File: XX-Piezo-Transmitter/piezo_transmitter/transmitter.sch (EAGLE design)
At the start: 5 parts, among them U1 BD6221FSOP, U2 ATTINY24A-SSUR

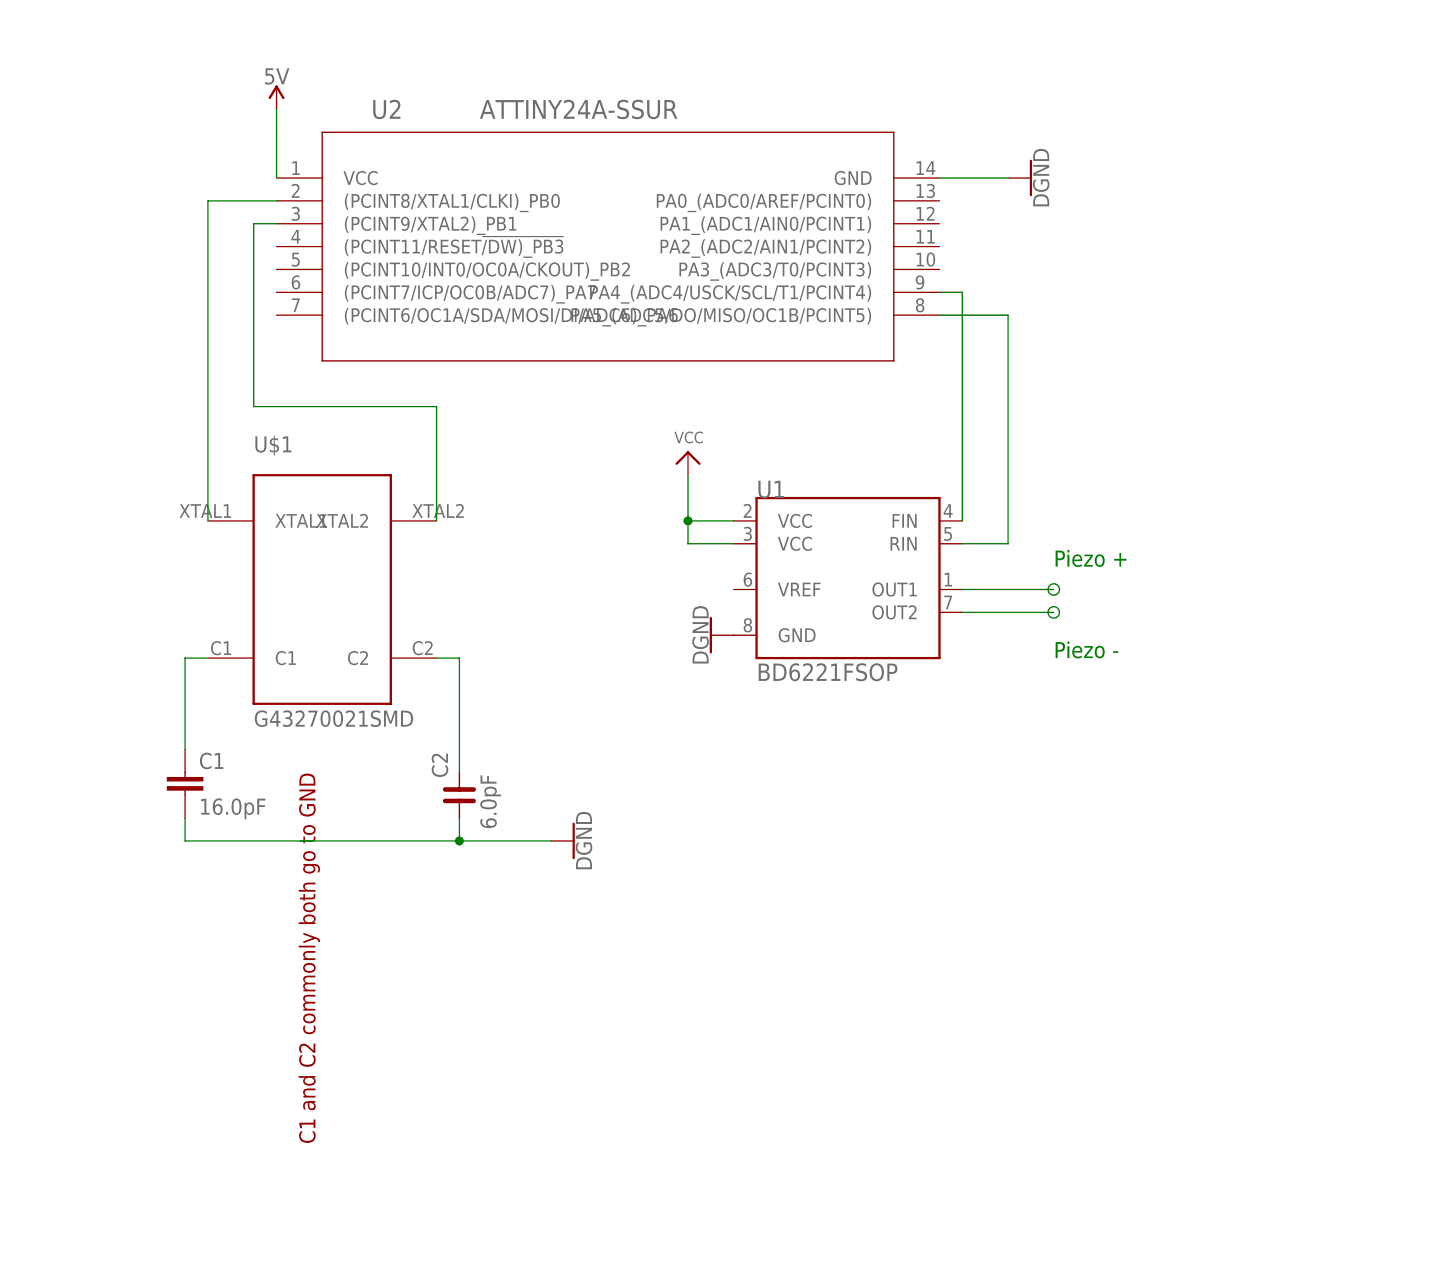
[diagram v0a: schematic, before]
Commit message: Added pin headers & pwm line, crystal and caps change.
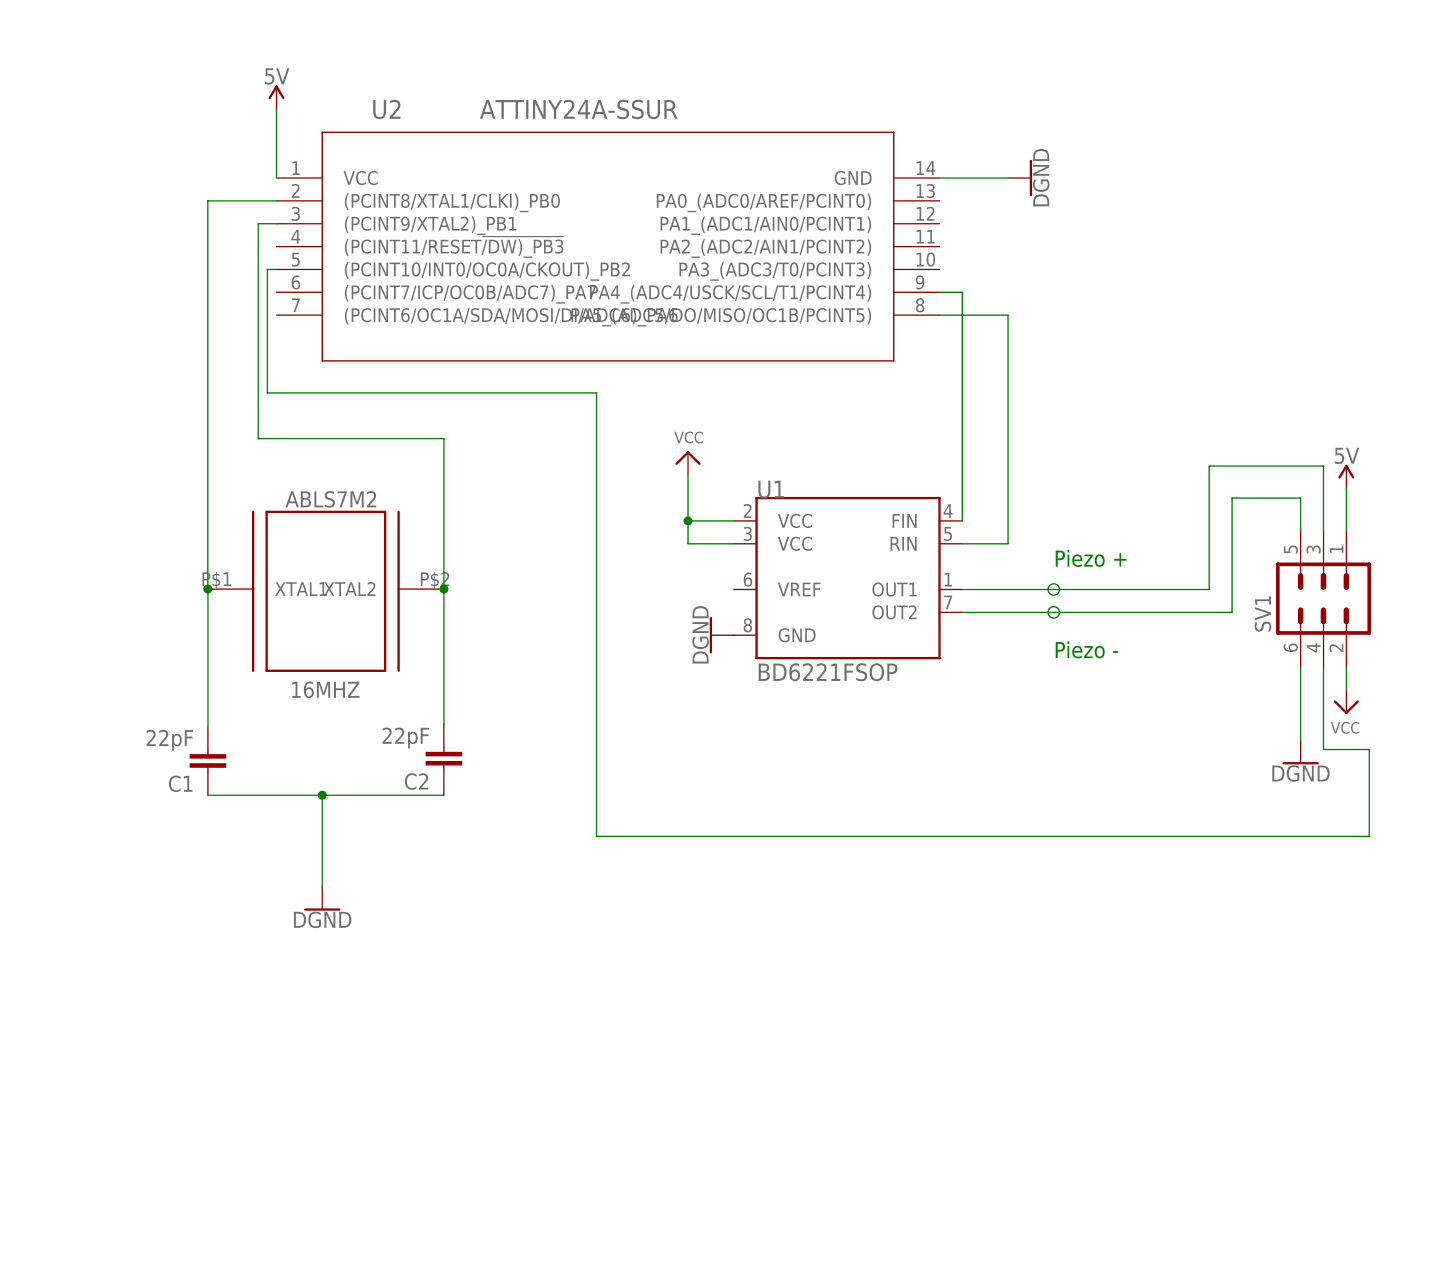
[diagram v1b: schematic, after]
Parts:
- added SV1: (no value), con-lstb:MA03-2
- C1: value 16.0pF -> 22pF; device SparkFun-Capacitors:9.0PF-0603-50V-10% -> SparkFun-Capacitors:22UF-0805-6.3V-20%
- C2: value 6.0pF -> 22pF; device rc-master-smd:C_0201 -> SparkFun-Capacitors:22UF-0805-6.3V-20%
- U$1: value G43270021SMD -> ABLS7M2-16; device G43270021 Oscillator:G43270021SMD -> ABLS7M2-16:ABLS7M2-16
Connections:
- net N$6 renamed FIN
- net N$7 renamed RIN
- removed net C1: C1.1, U$1.C1
- removed net C2: C2.2, U$1.C2
- removed net N$1: U$1.XTAL1, U2.(PCINT8/XTAL1/CLKI)_PB0
- removed net N$2: U$1.XTAL2, U2.(PCINT9/XTAL2)_PB1
- removed net N$5: U2.VCC
- removed net N$8: U1.OUT1
- removed net N$9: U1.OUT2
- new net PIEZO+: SV1.3, U1.OUT1
- new net PIEZO-: SV1.5, U1.OUT2
- new net PWM: SV1.4, U2.(PCINT10/INT0/OC0A/CKOUT)_PB2
- new net VCC_2: SV1.1, U2.VCC
- new net XTAL1: C1.2, U$1.XTAL1, U2.(PCINT8/XTAL1/CLKI)_PB0
- new net XTAL2: C2.2, U$1.XTAL2, U2.(PCINT9/XTAL2)_PB1
- net GND: now also C1.1, SV1.6; no longer C1.2
- net VCC: now also SV1.2
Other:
- moved on the sheet: C1, C2

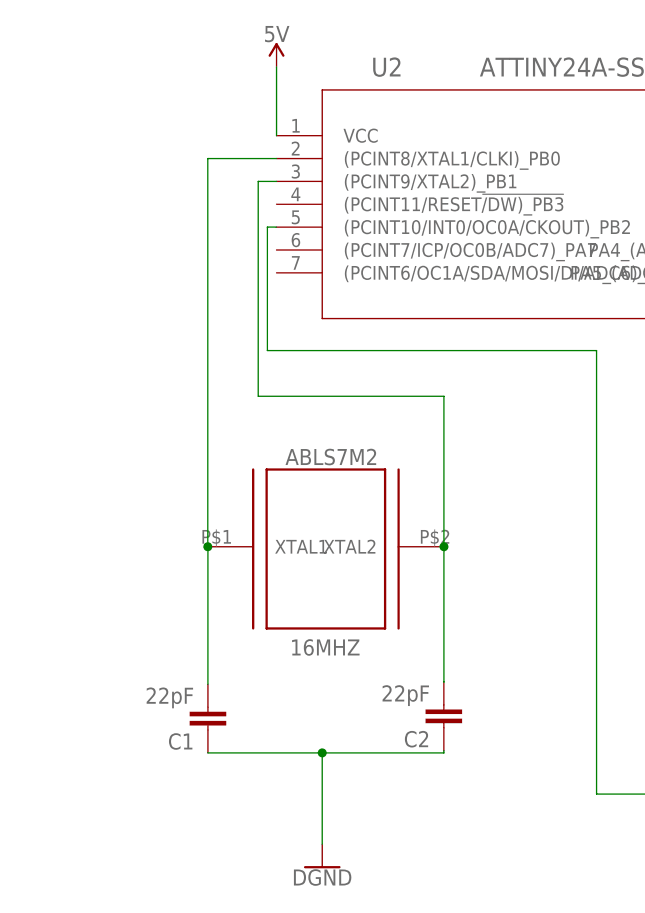
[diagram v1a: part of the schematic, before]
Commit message: Change to through hole crystal. Change to LV 22pf cap.
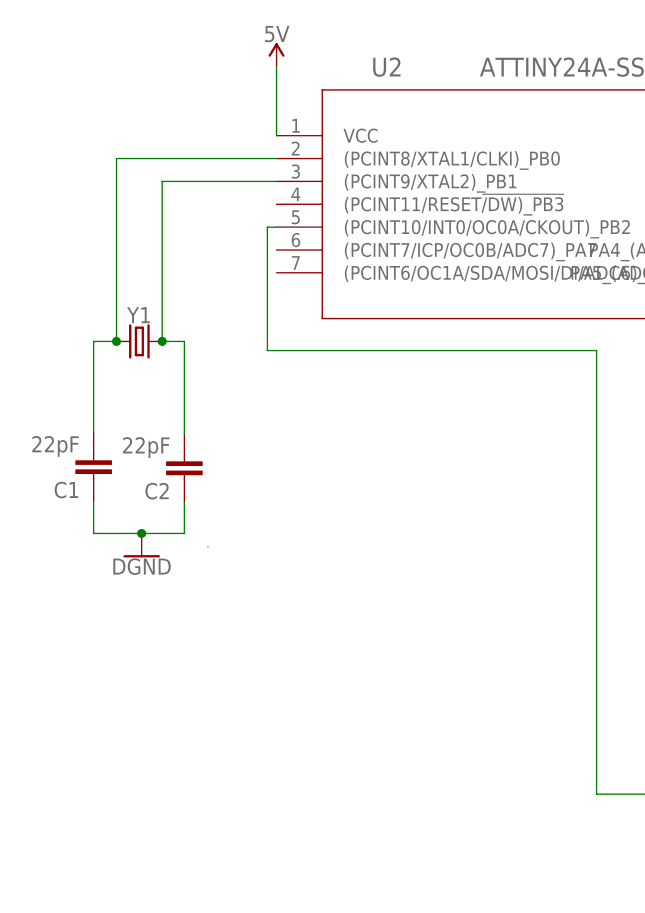
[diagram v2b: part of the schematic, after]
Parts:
- removed U$1: ABLS7M2-16, ABLS7M2-16:ABLS7M2-16
- added Y1: (no value), SparkFun-Clocks:CRYSTALPTH-HC49US
- C1, C2: device SparkFun-Capacitors:22UF-0805-6.3V-20% -> SparkFun-Retired:0.75PF-50V(-/+.25PF)(0603)
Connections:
- removed net XTAL1: C1.2, U$1.XTAL1, U2.(PCINT8/XTAL1/CLKI)_PB0
- removed net XTAL2: C2.2, U$1.XTAL2, U2.(PCINT9/XTAL2)_PB1
- new net N$2: C1.2, U2.(PCINT8/XTAL1/CLKI)_PB0, Y1.1
- new net N$3: C2.2, U2.(PCINT9/XTAL2)_PB1, Y1.2
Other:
- moved on the sheet: C1, C2
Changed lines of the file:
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@@
 <setting verticaltext="up"/>
 </settings>
-<grid distance="20" unitdist="mil" unit="mil" style="dots" multiple="1" display="yes" altdistance="0.01" altunitdist="inch" altunit="inch"/>
+<grid distance="10" unitdist="mil" unit="mil" style="dots" multiple="1" display="yes" altdistance="0.01" altunitdist="inch" altunit="inch"/>
 <layers>
 <layer number="1" name="Top" color="4" fill="1" visible="no" active="no"/>
@@
 <part name="GND2" library="SparkFun-PowerSymbols" library_urn="urn:adsk.eagle:library:530" deviceset="DGND" device=""/>
 <part name="GND3" library="SparkFun-PowerSymbols" library_urn="urn:adsk.eagle:library:530" deviceset="DGND" device=""/>
-<part name="U$1" library="ABLS7M2-16" deviceset="ABLS7M2-16" device=""/>
-<part name="C1" library="SparkFun-Capacitors" deviceset="22UF" device="-0805-6.3V-20%" value="22pF"/>
-<part name="C2" library="SparkFun-Capacitors" deviceset="22UF" device="-0805-6.3V-20%" value="22pF"/>
+<part name="C1" library="SparkFun-Retired" library_urn="urn:adsk.eagle:library:533" deviceset="0.75PF-50V(-/+.25PF)(0603)" device="" value="22pF"/>
+<part name="C2" library="SparkFun-Retired" library_urn="urn:adsk.eagle:library:533" deviceset="0.75PF-50V(-/+.25PF)(0603)" device="" value="22pF"/>
 <part name="GND1" library="SparkFun-PowerSymbols" library_urn="urn:adsk.eagle:library:530" deviceset="DGND" device=""/>
 <part name="SV1" library="con-lstb" library_urn="urn:adsk.eagle:library:162" deviceset="MA03-2" device="" package3d_urn="urn:adsk.eagle:package:8334/1"/>
@@
 <part name="GND4" library="SparkFun-PowerSymbols" library_urn="urn:adsk.eagle:library:530" deviceset="DGND" device=""/>
 <part name="5V1" library="SparkFun-PowerSymbols" library_urn="urn:adsk.eagle:library:530" deviceset="VCC_2" device="" value="5V"/>
+<part name="Y1" library="SparkFun-Clocks" library_urn="urn:adsk.eagle:library:511" deviceset="CRYSTAL" device="PTH-HC49US" package3d_urn="urn:adsk.eagle:package:37515/1"/>
 </parts>
 <sheets>
@@
 <instance part="GND2" gate="G$1" x="165.1" y="43.18" rot="R270"/>
 <instance part="GND3" gate="G$1" x="200.66" y="93.98" rot="R90"/>
-<instance part="U$1" gate="G$1" x="115.824" y="51.308"/>
-<instance part="C1" gate="G$1" x="109.22" y="30.48" rot="R180"/>
-<instance part="C2" gate="G$1" x="135.4328" y="30.734" rot="R180"/>
-<instance part="GND1" gate="G$1" x="121.92" y="12.7"/>
+<instance part="C1" gate="G$1" x="96.52" y="58.42" rot="R180"/>
+<instance part="C2" gate="G$1" x="106.6038" y="58.293" rot="R180"/>
+<instance part="GND1" gate="G$1" x="101.854" y="47.244"/>
 <instance part="SV1" gate="1" x="233.172" y="47.244" rot="R90"/>
 <instance part="P+2" gate="VCC" x="235.712" y="34.544" rot="R180"/>
 <instance part="GND4" gate="G$1" x="230.632" y="28.956"/>
 <instance part="5V1" gate="G$1" x="235.712" y="59.436"/>
+<instance part="Y1" gate="G$1" x="101.6" y="71.12"/>
 </instances>
 <busses>
@@
 </segment>
 <segment>
-<pinref part="C1" gate="G$1" pin="1"/>
-<pinref part="C2" gate="G$1" pin="1"/>
-<wire x1="109.22" y1="25.4" x2="121.92" y2="25.4" width="0.1524" layer="91"/>
-<wire x1="121.92" y1="25.4" x2="135.4328" y2="25.4" width="0.1524" layer="91"/>
-<wire x1="135.4328" y1="25.4" x2="135.4328" y2="25.654" width="0.1524" layer="91"/>
-<pinref part="GND1" gate="G$1" pin="GND"/>
-<wire x1="121.92" y1="15.24" x2="121.92" y2="25.4" width="0.1524" layer="91"/>
-<junction x="121.92" y="25.4"/>
-</segment>
-<segment>
 <pinref part="SV1" gate="1" pin="6"/>
 <pinref part="GND4" gate="G$1" pin="GND"/>
 <wire x1="230.632" y1="39.624" x2="230.632" y2="31.496" width="0.1524" layer="91"/>
+</segment>
+<segment>
+<pinref part="C1" gate="G$1" pin="1"/>
+<pinref part="GND1" gate="G$1" pin="GND"/>
+<wire x1="96.52" y1="53.34" x2="96.52" y2="49.784" width="0.1524" layer="91"/>
+<wire x1="96.52" y1="49.784" x2="101.854" y2="49.784" width="0.1524" layer="91"/>
+<pinref part="C2" gate="G$1" pin="1"/>
+<wire x1="101.854" y1="49.784" x2="106.6038" y2="49.784" width="0.1524" layer="91"/>
+<wire x1="106.6038" y1="49.784" x2="106.6038" y2="53.213" width="0.1524" layer="91"/>
+<junction x="101.854" y="49.784"/>
 </segment>
 </net>
@@
 <wire x1="198.12" y1="53.34" x2="198.12" y2="78.74" width="0.1524" layer="91"/>
 <wire x1="198.12" y1="78.74" x2="190.5" y2="78.74" width="0.1524" layer="91"/>
-</segment>
-</net>
-<net name="XTAL1" class="0">
-<segment>
-<pinref part="U2" gate="A" pin="(PCINT8/XTAL1/CLKI)_PB0"/>
-<pinref part="U$1" gate="G$1" pin="XTAL1"/>
-<wire x1="116.84" y1="91.44" x2="109.204" y2="91.44" width="0.1524" layer="91"/>
-<wire x1="109.204" y1="91.44" x2="109.204" y2="48.308" width="0.1524" layer="91"/>
-<pinref part="C1" gate="G$1" pin="2"/>
-<wire x1="109.204" y1="48.308" x2="109.22" y2="48.308" width="0.1524" layer="91"/>
-<wire x1="109.22" y1="48.308" x2="109.22" y2="33.02" width="0.1524" layer="91"/>
-<junction x="109.204" y="48.308"/>
-</segment>
-</net>
-<net name="XTAL2" class="0">
-<segment>
-<pinref part="U2" gate="A" pin="(PCINT9/XTAL2)_PB1"/>
-<wire x1="116.84" y1="88.9" x2="114.808" y2="88.9" width="0.1524" layer="91"/>
-<wire x1="114.808" y1="88.9" x2="114.808" y2="65.024" width="0.1524" layer="91"/>
-<pinref part="U$1" gate="G$1" pin="XTAL2"/>
-<wire x1="114.808" y1="65.024" x2="135.444" y2="65.024" width="0.1524" layer="91"/>
-<wire x1="135.444" y1="65.024" x2="135.444" y2="48.308" width="0.1524" layer="91"/>
-<pinref part="C2" gate="G$1" pin="2"/>
-<wire x1="135.444" y1="48.308" x2="135.444" y2="33.274" width="0.1524" layer="91"/>
-<wire x1="135.444" y1="33.274" x2="135.4328" y2="33.274" width="0.1524" layer="91"/>
-<junction x="135.444" y="48.308"/>
 </segment>
 </net>
@@
 </segment>
 </net>
+<net name="N$1" class="0">
+<segment>
+<wire x1="109.204" y1="48.308" x2="109.22" y2="48.308" width="0.1524" layer="91"/>
+</segment>
+</net>
+<net name="N$2" class="0">
+<segment>
+<pinref part="U2" gate="A" pin="(PCINT8/XTAL1/CLKI)_PB0"/>
+<pinref part="Y1" gate="G$1" pin="1"/>
+<wire x1="116.84" y1="91.44" x2="99.06" y2="91.44" width="0.1524" layer="91"/>
+<wire x1="99.06" y1="91.44" x2="99.06" y2="71.12" width="0.1524" layer="91"/>
+<pinref part="C1" gate="G$1" pin="2"/>
+<wire x1="99.06" y1="71.12" x2="96.52" y2="71.12" width="0.1524" layer="91"/>
+<wire x1="96.52" y1="71.12" x2="96.52" y2="60.96" width="0.1524" layer="91"/>
+<junction x="99.06" y="71.12"/>
+</segment>
+</net>
+<net name="N$3" class="0">
+<segment>
+<pinref part="U2" gate="A" pin="(PCINT9/XTAL2)_PB1"/>
+<pinref part="Y1" gate="G$1" pin="2"/>
+<wire x1="116.84" y1="88.9" x2="104.14" y2="88.9" width="0.1524" layer="91"/>
+<wire x1="104.14" y1="88.9" x2="104.14" y2="71.12" width="0.1524" layer="91"/>
+<pinref part="C2" gate="G$1" pin="2"/>
+<wire x1="104.14" y1="71.12" x2="106.6038" y2="71.12" width="0.1524" layer="91"/>
+<wire x1="106.6038" y1="71.12" x2="106.6038" y2="60.833" width="0.1524" layer="91"/>
+<junction x="104.14" y="71.12"/>
+</segment>
+</net>
